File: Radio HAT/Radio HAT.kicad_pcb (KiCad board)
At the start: 2 copper layers, 65 x 35 mm, 16 parts, among them J1 Raspberry_Pi_2_3, J2 Coax SMA, J3 Barrel_Jack, J4 Testpoints, U1 RFM98PW, U2 AZ2185D-ADJTRG1

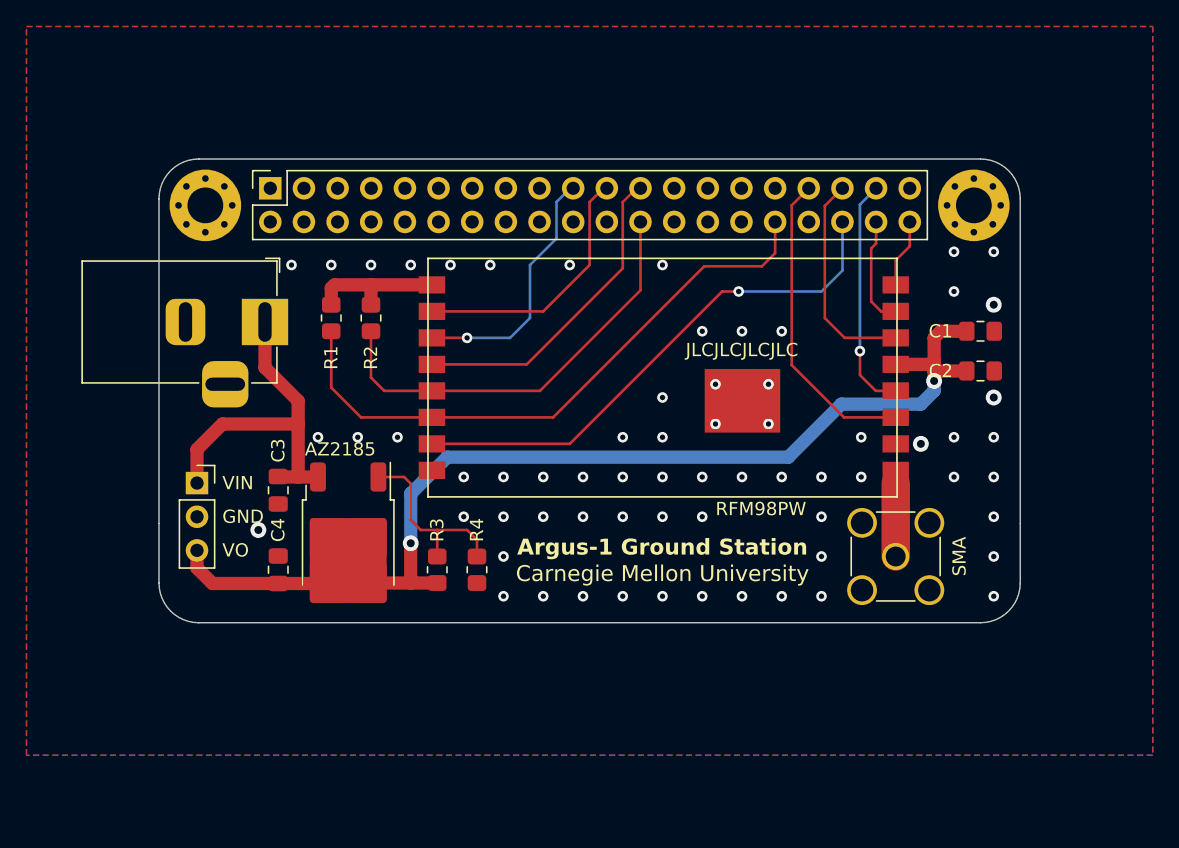
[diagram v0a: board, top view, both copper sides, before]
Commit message: Changed connector orientation
Changed orientation of 40-pin connector, increased board size, added optional pot, added graphics
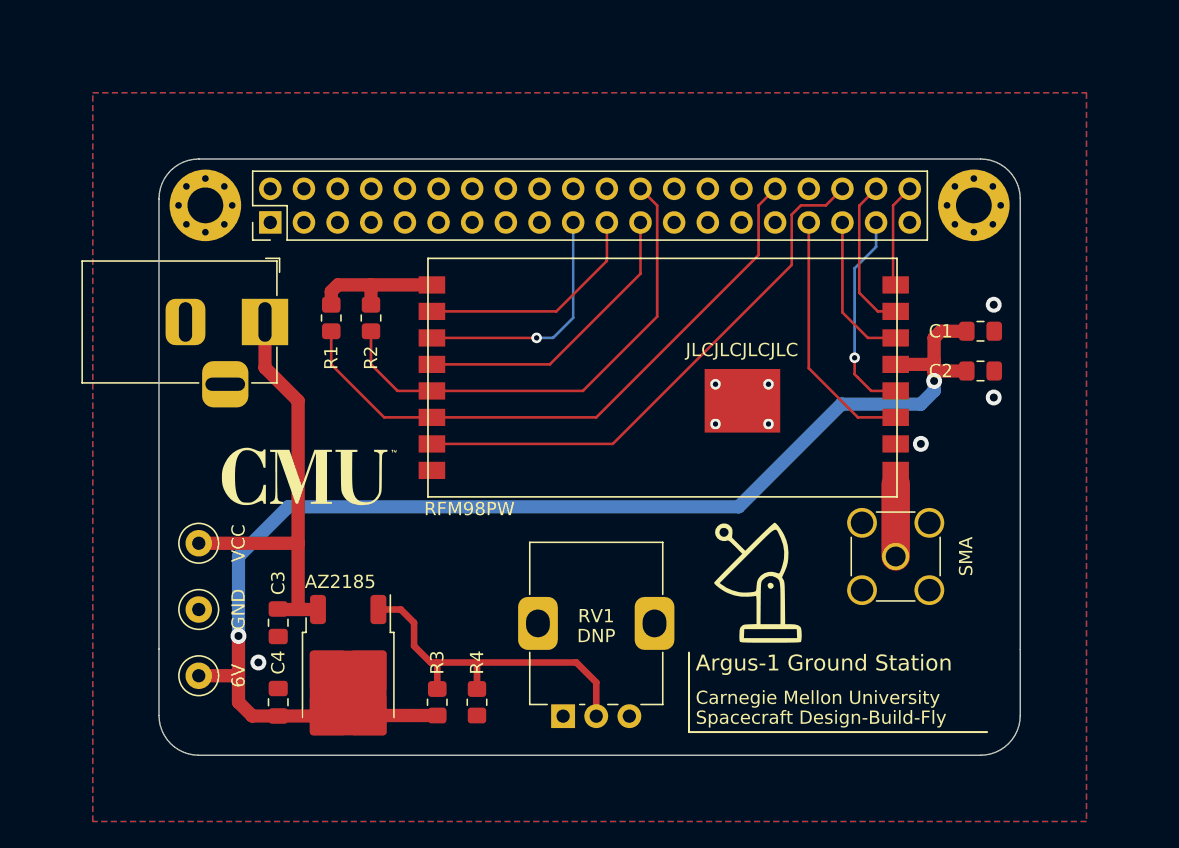
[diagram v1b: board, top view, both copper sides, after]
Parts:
- added G***: LOGO, LOGO, F.Cu at (145.2, 132.0)
- added G***: LOGO, LOGO, F.Cu at (111.0, 124.0)
- added J5: 6V, TestPoint:TestPoint_Loop_D2.50mm_Drill1.0mm, F.Cu at (103.0, 139.0)
- added J6: GND, TestPoint:TestPoint_Loop_D2.50mm_Drill1.0mm, F.Cu at (103.0, 134.0)
- added RV1: RK09K1130A8G, Potentiometer_THT:Potentiometer_Alps_RK09K_Single_Vertical, F.Cu at (130.5, 142.1)
- J4: value Testpoints -> VCC; footprint Connector_PinSocket_2.54mm:PinSocket_1x03_P2.54mm_Vertical -> TestPoint:TestPoint_Loop_D2.50mm_Drill1.0mm
- R4: value 3.74K -> 1.1K
- moved C3 10.0 mm to (109.0, 135.0)
- moved C4 10.0 mm to (109.0, 141.0)
- moved R3 10.0 mm to (121.0, 141.0)
- moved R4 10.0 mm to (124.0, 141.0)
- moved U2 10.0 mm to (114.3, 139.0)
- moved J4 4.54 mm to (103.0, 129.0)
- moved J1 2.58 mm to (108.4, 104.8)
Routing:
- net +6V: track 78.5 -> 96.2 mm
- net /REG_ADJ: track 14.3 -> 26.3 mm
- net VCC: track 26.8 -> 33.3 mm
- net /RF_CS: track 32.6 -> 37.4 mm
- net /RF_DIO0: track 16.3 -> 11.6 mm
- net /RF_DIO3: track 23.4 -> 19.1 mm
- net /RF_DIO1: track 8.31 -> 11.7 mm
- net /RF_DIO2: track 5.19 -> 7.85 mm
- net /RF_MISO: track 19.8 -> 17.7 mm
- net /RF_DIO4: track 17.8 -> 15.7 mm
- net /RF_SCK: track 24.2 -> 22.4 mm
- net /RF_DIO5: track 40.1 -> 41.5 mm, vias 1 -> 0
- net /RF_RESET: track 46.2 -> 47.0 mm
- net /RF_MOSI: track 19.3 -> 18.5 mm
- net GND: vias 66 -> 8
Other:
- board size 65 x 35 mm -> 65 x 45 mm
- board text added: "6V"
- board text added: "Argus-1 Groundstation v1.1"
- board text added: "DNP"
- board text added: "Spacecraft Design-Build-Fly"
- board text added: "VCC"
- board text removed: "Argus-1 Groundstation v1.0"
- board text removed: "VIN"
- board text removed: "VO"

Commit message: Implemented PR feedback by Jason
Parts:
- added R5: 0, Resistor_SMD:R_1206_3216Metric_Pad1.30x1.75mm_HandSolder, F.Cu at (116.0, 128.0)
- added R6: 0, Resistor_SMD:R_0805_2012Metric_Pad1.20x1.40mm_HandSolder, F.Cu at (124.0, 132.0)
- C1, C2: footprint Capacitor_SMD:C_0805_2012Metric_Pad1.18x1.45mm_HandSolder -> Capacitor_SMD:C_0603_1608Metric_Pad1.08x0.95mm_HandSolder
- R1, R2: value 10k -> 10K
- R3: value 1.1K -> 2.8K
- R4: value 1.1K -> 10K
- moved C1 2.55 mm to (159.5, 112.5)
- moved C2 2.55 mm to (159.5, 115.5)
- moved G*** 0.25 mm to (145.0, 132.0)
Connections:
- C1 pad 1: +6V -> /V_RF
- C2 pad 1: +6V -> /V_RF
- RV1 pad 2: /REG_ADJ -> Net-(R6-Pad2)
- U1 pad 5: +6V -> /V_RF
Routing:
- net /V_RF: track 0.00 -> 77.6 mm
- net +6V: track 96.2 -> 35.6 mm
- net Net-(R6-Pad2): track 0.00 -> 18.9 mm
- net /REG_ADJ: track 26.3 -> 19.1 mm
- net VCC: track 33.3 -> 35.6 mm
- net /RF_DIO5: track 41.5 -> 39.5 mm
- net /RF_RESET: track 47.0 -> 45.8 mm
- net /RF_CS: track 37.4 -> 36.2 mm
- net /RF_DIO3: track 19.1 -> 18.1 mm
- net GND: vias 8 -> 0
- added copper zone on F.Cu, net /V_RF

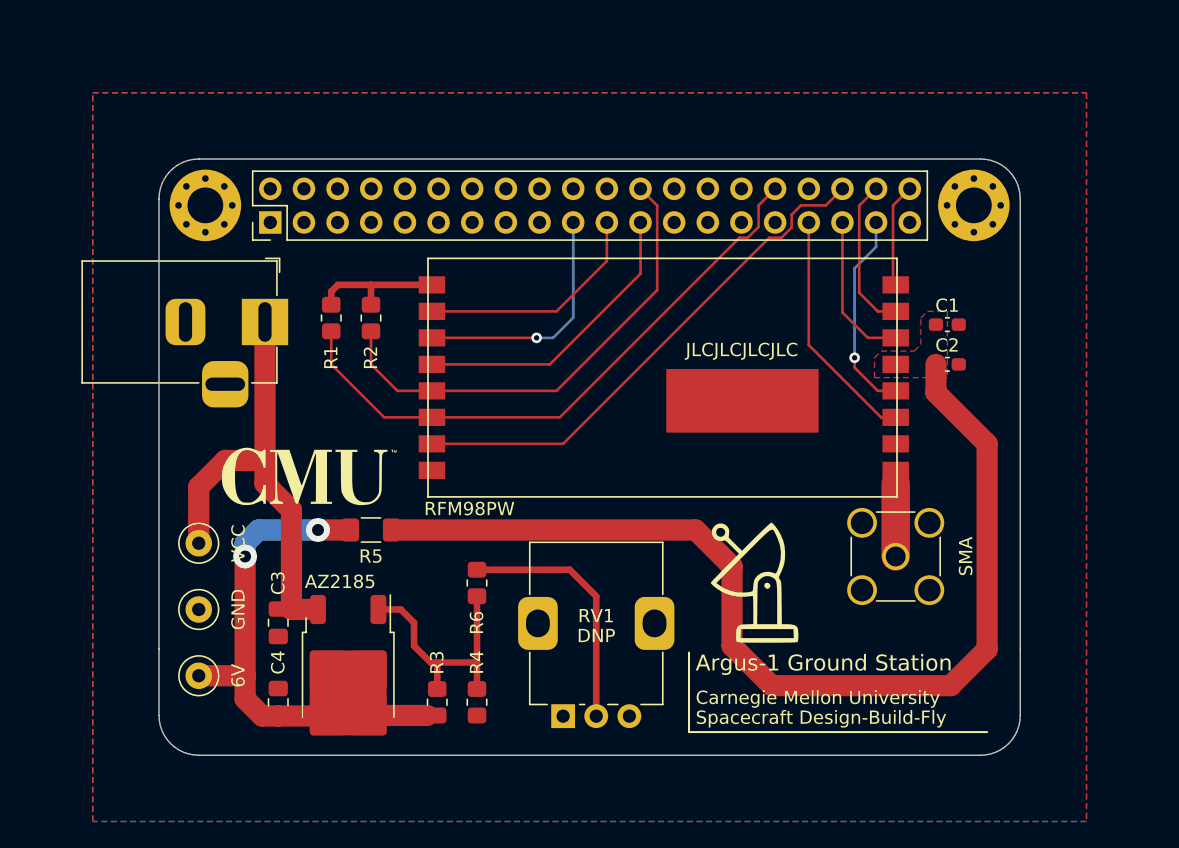
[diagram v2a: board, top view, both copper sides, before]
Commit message: Updated schematic, changed power routing
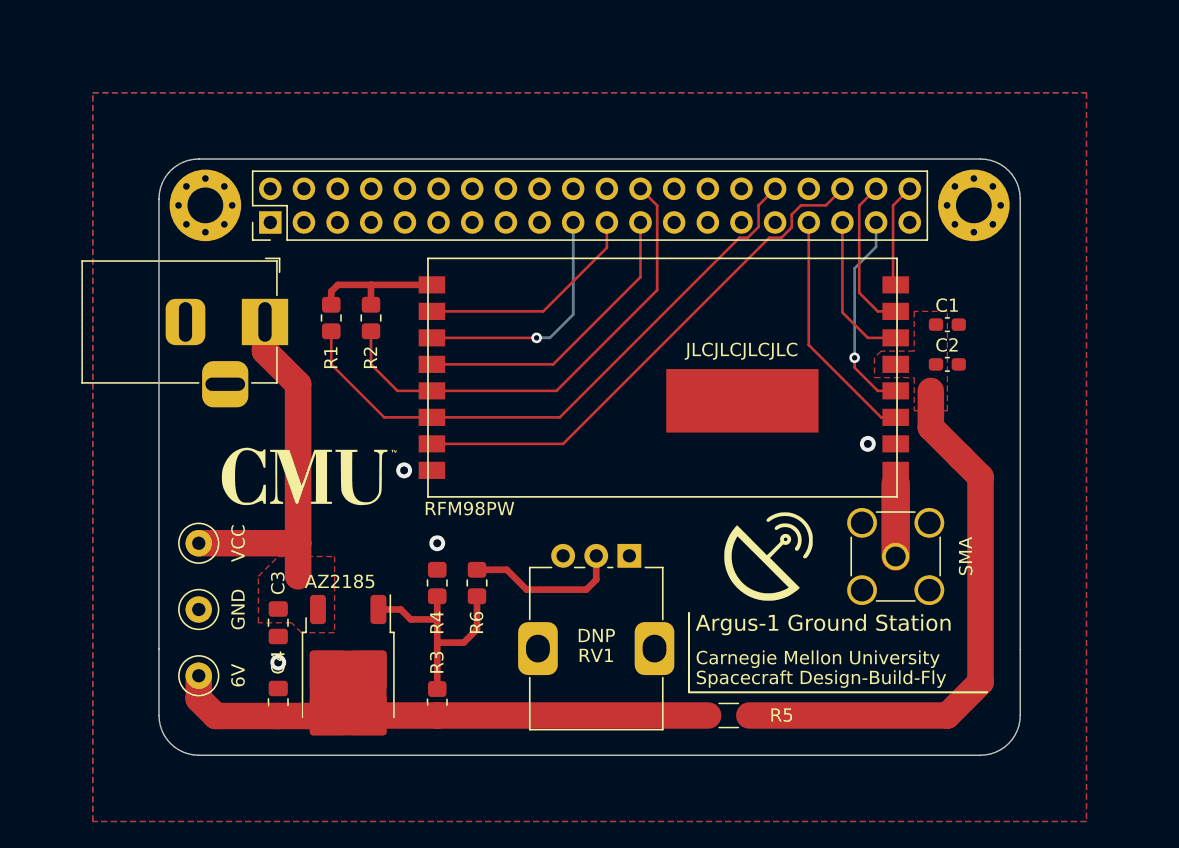
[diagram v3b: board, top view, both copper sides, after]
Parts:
- moved R5 30.4 mm to (143.0, 142.0)
- moved RV1 13.1 mm to (135.5, 129.9), turned to -90 degrees
- moved R4 9.49 mm to (121.0, 132.0), turned to 90 degrees
- moved G*** 2.24 mm to (146.0, 130.0)
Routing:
- net /V_RF: track 77.6 -> 42.0 mm
- net VCC: track 35.6 -> 27.8 mm
- net Net-(R6-Pad2): track 18.9 -> 11.7 mm
- net +6V: track 35.6 -> 37.7 mm, vias 2 -> 0
- net /REG_ADJ: track 19.1 -> 17.7 mm
- net /RF_MISO: track 17.7 -> 17.1 mm
- net GND: vias 0 -> 4
- added copper zone on F.Cu, net VCC

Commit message: Reworked power traces, added stitching vias
Reworked 3V3 net, added stitching vias on board, added passive components, regenerated BOM and STEP file for board
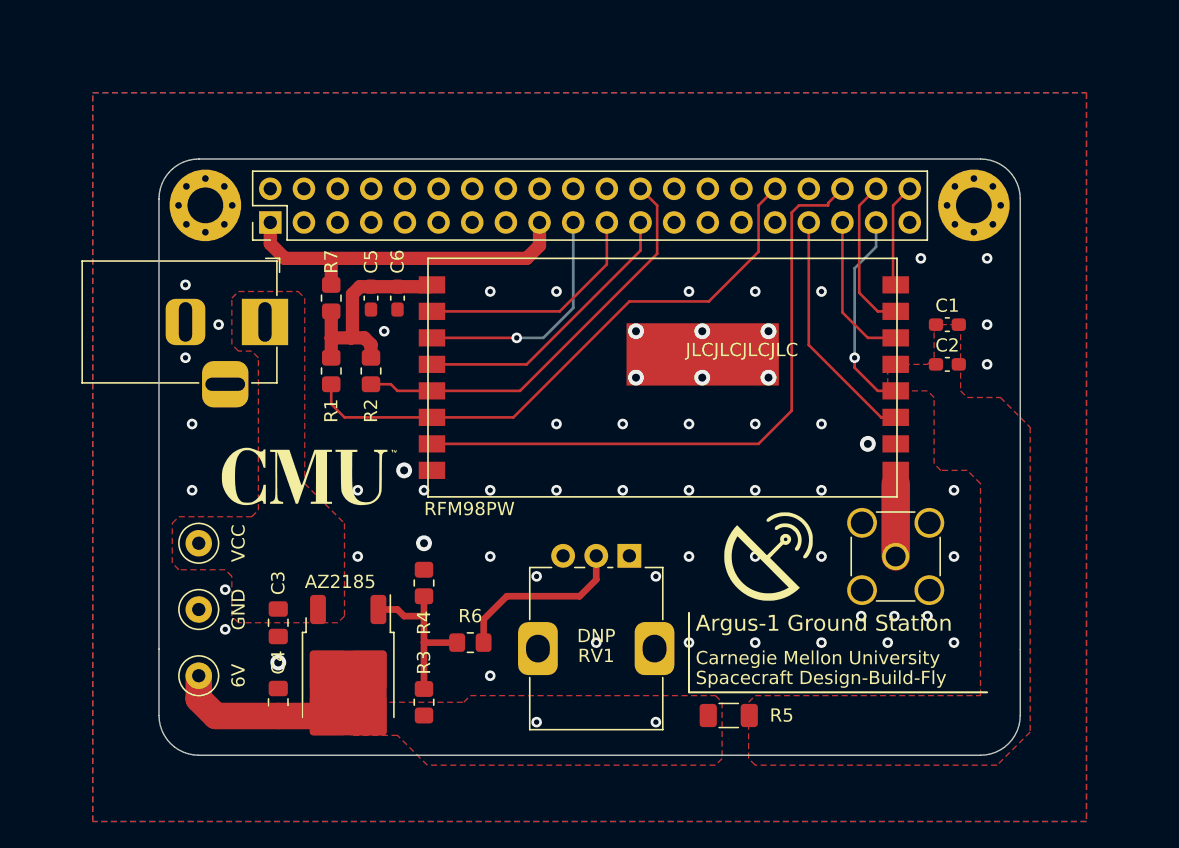
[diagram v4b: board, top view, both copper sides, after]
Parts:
- added C5: DNP, Capacitor_SMD:C_0603_1608Metric_Pad1.08x0.95mm_HandSolder, F.Cu at (116.0, 110.5)
- added C6: DNP, Capacitor_SMD:C_0603_1608Metric_Pad1.08x0.95mm_HandSolder, F.Cu at (118.0, 110.5)
- added R7: DNP, Resistor_SMD:R_0805_2012Metric_Pad1.20x1.40mm_HandSolder, F.Cu at (113.0, 110.5)
- R6: value 0 -> DNP
- moved R6 4.53 mm to (123.5, 136.5), turned to 0 degrees
- moved R1 4.00 mm to (113.0, 116.0)
- moved R2 4.00 mm to (116.0, 116.0)
- moved R3 1.00 mm to (120.0, 141.0)
- moved R4 1.00 mm to (120.0, 132.0)
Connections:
- net Net-(R6-Pad2) renamed /REG_POT
- J1 pad 1: unconnected-(J1-3V3-Pad1) -> /RPI_3V3
- J1 pad 17: unconnected-(J1-3V3-Pad17) -> /RPI_3V3
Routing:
- net /V_RF: track 42.0 -> 0.00 mm
- net VCC: track 27.8 -> 0.05 mm
- net /RPI_3V3: track 0.00 -> 26.5 mm
- net +6V: track 37.7 -> 12.1 mm, vias 0 -> 2
- net /RF_DIO5: track 39.5 -> 47.8 mm
- net +3V3: track 10.3 -> 17.3 mm
- net /RF_CS: track 36.2 -> 31.5 mm
- net /REG_ADJ: track 17.7 -> 13.1 mm
- net /REG_POT: track 11.7 -> 13.3 mm
- net /RF_SCK: track 22.6 -> 21.4 mm
- net /RF_RESET: track 45.8 -> 44.6 mm
- net /RF_MISO: track 17.1 -> 17.8 mm
- net GND: vias 4 -> 59
- added copper zone on F.Cu, net +6V
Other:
- board text removed: "SMA"
